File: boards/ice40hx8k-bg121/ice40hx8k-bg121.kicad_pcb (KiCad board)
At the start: 4 copper layers, 22.9 x 48.3 mm, 56 parts, among them J1 Conn_01x16, J2 Conn_01x16, J3 Conn_02x06_Odd_Even, J4 Conn_02x06_Odd_Even, SW1 B3U-1000P, U1 AP7361C-33Y5-13, U2 AP7361C-12Y5-13, U3 iCE40HX8K-BG121(121-Ball_caBG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, U4 LE25U20AMB, U5 ASDMB-xxxMHz

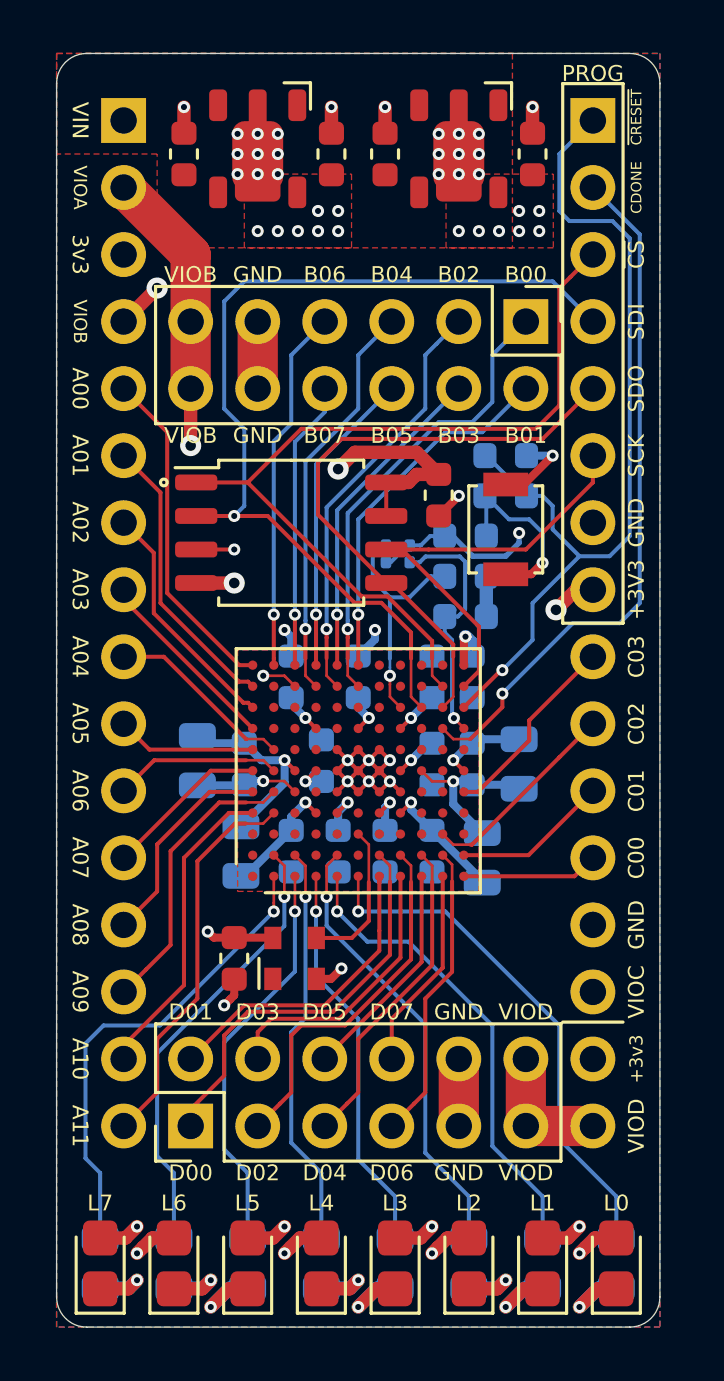
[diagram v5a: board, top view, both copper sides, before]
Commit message: Revert "Updated version info on backside of board."
This reverts commit 1f51933b87c9f3e20d21da3a8fb08a06faebd8ba.
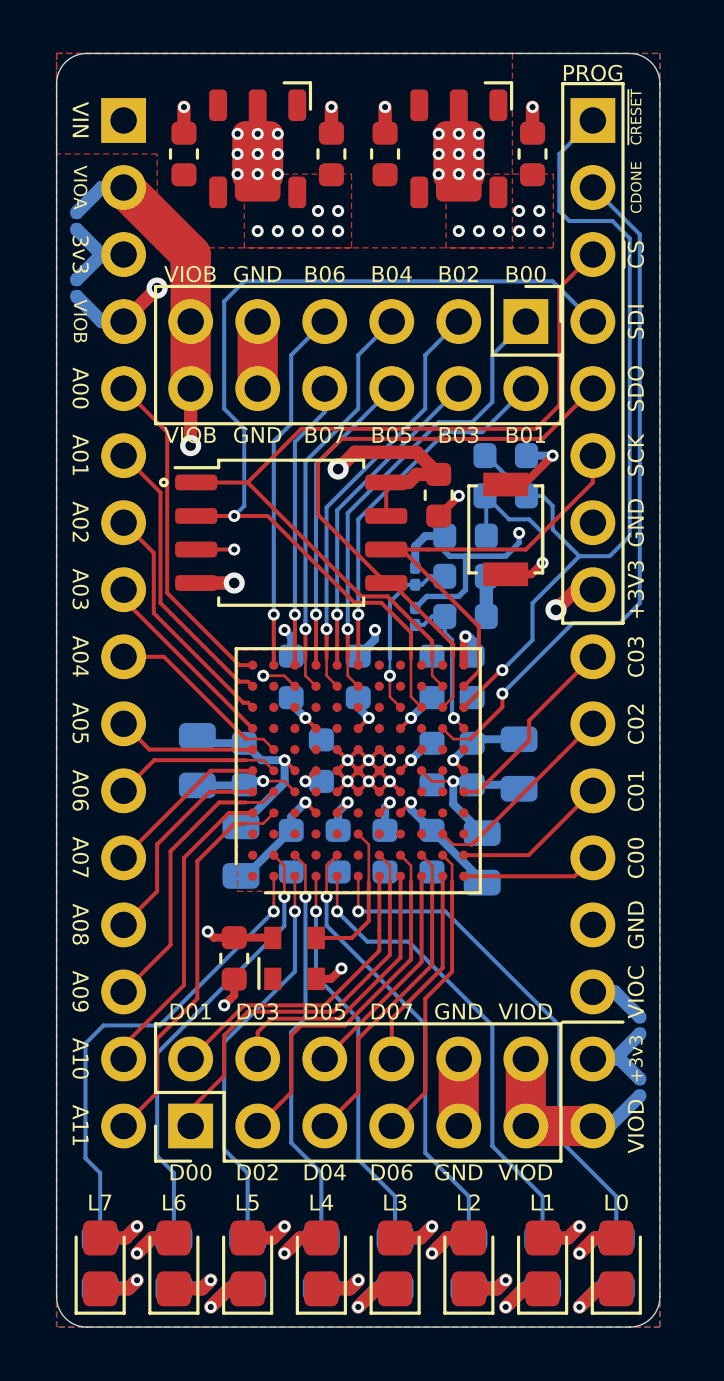
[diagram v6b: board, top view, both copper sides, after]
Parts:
- added JP3: VCCIO_A, jkiv-library:J_NO_0201_0603Metric, B.Cu at (21.1, 24.1)
- added JP4: VCCIO_B, jkiv-library:J_NO_0201_0603Metric, B.Cu at (21.1, 21.6)
- added JP5: VCCIO_C, jkiv-library:J_NO_0201_0603Metric, B.Cu at (42.4, 52.1)
- added JP6: VCCIO_D, jkiv-library:J_NO_0201_0603Metric, B.Cu at (42.4, 54.4)
- moved JP1 2.39 mm to (33.9, 36.6)
- moved JP2 1.40 mm to (33.9, 35.1), turned to 270 degrees
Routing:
- net +3V3: track 36.1 -> 47.1 mm
- net CBSEL0: track 9.55 -> 5.84 mm
- net CBSEL1: track 9.35 -> 6.63 mm
- net VCCIO_D: track 23.3 -> 25.5 mm
- net VCCIO_C: track 15.9 -> 18.1 mm
- net VCCIO_B: track 28.3 -> 30.4 mm
- net VCCIO_A: track 25.4 -> 27.5 mm
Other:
- board text added: "fourside.io"
- board text added: "ice40hx8k breakout 2020-03"
- board text removed: "(cc) fourside.io"
- board text removed: "ice40hx8k breakout 2020-04"

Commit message: [ice40hx8k-bg121] Updated design rules. Passes DRC.
Updated design rules. Adjusted soldermask clearance ratio.
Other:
- rule trace_min: 0.0889 -> 0.09
- rule via_min_size: 0.23 -> 0.45
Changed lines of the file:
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@@
     (zone_clearance 0.1016)
     (zone_45_only no)
-    (trace_min 0.0889)
+    (trace_min 0.09)
     (via_size 0.8)
     (via_drill 0.4)
-    (via_min_size 0.23)
+    (via_min_size 0.45)
     (via_min_drill 0.2)
     (user_via 0.4572 0.2286)
@@
     (pad_to_mask_clearance 0.051)
     (solder_mask_min_width 0.25)
+    (pad_to_paste_clearance_ratio -0.15)
     (aux_axis_origin 0 0)
     (visible_elements 7FFFFFFF)
@@
     (add_net VCCIO_D)
   )
+  (module jkiv-library:J_NO_0201_0603Metric (layer B.Cu)
+    (at 33.909 35.052 270)
+    (descr "Resistor SMD 0201 (0603 Metric), square (rectangular) end terminal, IPC_7351 nominal, (Body size source: https://www.vishay.com/docs/20052/crcw0201e3.pdf), generated with kicad-footprint-generator")
+    (tags resistor)
+    (attr smd)
+    (fp_text reference JP2 (at 0 0.254 90) (layer B.SilkS) hide
+      (effects (font (size 1 1) (thickness 0.15)) (justify mirror))
+    )
+    (fp_text value CBSEL0 (at 0 -1.05 90) (layer B.Fab)
+      (effects (font (size 1 1) (thickness 0.15)) (justify mirror))
+    )
+    (fp_line (start -0.6 -0.3) (end -0.6 0.3) (layer B.SilkS) (width 0.12))
+    (fp_line (start 0.6 -0.3) (end -0.6 -0.3) (layer B.SilkS) (width 0.12))
+    (fp_line (start 0.6 0.3) (end 0.6 -0.3) (layer B.SilkS) (width 0.12))
+    (fp_line (start -0.6 0.3) (end 0.6 0.3) (layer B.SilkS) (width 0.12))
+    (fp_poly (pts (xy -0.2 0.1) (xy 0.2 0.1) (xy 0.2 -0.1) (xy -0.2 -0.1)) (layer B.Mask) (width 0.1))
+    (fp_text user %R (at 0 0.68 90) (layer B.Fab)
+      (effects (font (size 0.25 0.25) (thickness 0.04)) (justify mirror))
+    )
+    (fp_line (start 0.3 0.15) (end 0.3 -0.15) (layer B.Fab) (width 0.1))
+    (fp_line (start -0.3 -0.15) (end -0.3 0.15) (layer B.Fab) (width 0.1))
+    (pad 2 smd roundrect (at 0.32 0 270) (size 0.46 0.4) (layers B.Cu B.Mask) (roundrect_rratio 0.25)
+      (net 98 CBSEL1) (solder_paste_margin_ratio -0.5))
+    (pad 1 smd roundrect (at -0.32 0 270) (size 0.46 0.4) (layers B.Cu B.Mask) (roundrect_rratio 0.25)
+      (net 2 +3V3) (solder_paste_margin_ratio -0.5))
+    (pad "" smd roundrect (at 0.345 0 270) (size 0.318 0.36) (layers B.Paste) (roundrect_rratio 0.25))
+    (pad "" smd roundrect (at -0.345 0 270) (size 0.318 0.36) (layers B.Paste) (roundrect_rratio 0.25))
+  )
   (module Symbol:OSHW-Symbol_6.7x6mm_SilkScreen (layer B.Cu)
     (at 31.75 19.558 180)
@@
   )
   (module jkiv-library:J_NO_0201_0603Metric (layer B.Cu)
-    (at 33.909 35.052 270)
-    (descr "Resistor SMD 0201 (0603 Metric), square (rectangular) end terminal, IPC_7351 nominal, (Body size source: https://www.vishay.com/docs/20052/crcw0201e3.pdf), generated with kicad-footprint-generator")
-    (tags resistor)
-    (attr smd)
-    (fp_text reference JP2 (at 0 0.254 90) (layer B.SilkS) hide
-      (effects (font (size 1 1) (thickness 0.15)) (justify mirror))
-    )
-    (fp_text value CBSEL0 (at 0 -1.05 90) (layer B.Fab)
-      (effects (font (size 1 1) (thickness 0.15)) (justify mirror))
-    )
-    (fp_line (start -0.6 -0.3) (end -0.6 0.3) (layer B.SilkS) (width 0.12))
-    (fp_line (start 0.6 -0.3) (end -0.6 -0.3) (layer B.SilkS) (width 0.12))
-    (fp_line (start 0.6 0.3) (end 0.6 -0.3) (layer B.SilkS) (width 0.12))
-    (fp_line (start -0.6 0.3) (end 0.6 0.3) (layer B.SilkS) (width 0.12))
-    (fp_poly (pts (xy -0.2 0.1) (xy 0.2 0.1) (xy 0.2 -0.1) (xy -0.2 -0.1)) (layer B.Mask) (width 0.1))
-    (fp_text user %R (at 0 0.68 90) (layer B.Fab)
-      (effects (font (size 0.25 0.25) (thickness 0.04)) (justify mirror))
-    )
-    (fp_line (start 0.3 0.15) (end 0.3 -0.15) (layer B.Fab) (width 0.1))
-    (fp_line (start -0.3 -0.15) (end -0.3 0.15) (layer B.Fab) (width 0.1))
-    (pad 2 smd roundrect (at 0.32 0 270) (size 0.46 0.4) (layers B.Cu B.Mask) (roundrect_rratio 0.25)
-      (net 98 CBSEL1) (solder_paste_margin_ratio -0.5))
-    (pad 1 smd roundrect (at -0.32 0 270) (size 0.46 0.4) (layers B.Cu B.Mask) (roundrect_rratio 0.25)
-      (net 2 +3V3) (solder_paste_margin_ratio -0.5))
-    (pad "" smd roundrect (at 0.345 0 270) (size 0.318 0.36) (layers B.Paste) (roundrect_rratio 0.25))
-    (pad "" smd roundrect (at -0.345 0 270) (size 0.318 0.36) (layers B.Paste) (roundrect_rratio 0.25))
-  )
-  (module jkiv-library:J_NO_0201_0603Metric (layer B.Cu)

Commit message: Updated sheet info, gerbers, BOMs.
* ft2232h-ice40
* ice40hx8k-bg121 breakout
* atsamd21e18a
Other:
- board text added: "ice40hx8k breakout 2020-04"
- board text removed: "ice40hx8k breakout 2020-03"
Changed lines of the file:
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@@
   )
   (page A4)
+  (title_block
+    (title "ice40hx8k-bg121 Breakout")
+    (date 2020-11-09)
+    (rev 2020-04)
+    (company fourside.io)
+  )
   (layers
     (0 F.Cu signal)
@@
     (pcbplotparams
       (layerselection 0x010fc_ffffffff)
-      (usegerberextensions true)
+      (usegerberextensions false)
       (usegerberattributes false)
-      (usegerberadvancedattributes true)
+      (usegerberadvancedattributes false)
       (creategerberjobfile false)
       (excludeedgelayer true)
@@
       (psa4output false)
       (plotreference true)
-      (plotvalue true)
+      (plotvalue false)
       (plotinvisibletext false)
-      (padsonsilk false)
+      (padsonsilk true)
       (subtractmaskfromsilk true)
       (outputformat 1)
@@
     (effects (font (size 0.4 0.4) (thickness 0.1)) (justify mirror))
   )
-  (gr_text "ice40hx8k breakout\n2020-03" (at 31.623 50.546) (layer B.SilkS)
+  (gr_text "ice40hx8k breakout\n2020-04" (at 31.623 50.546) (layer B.SilkS)
     (effects (font (size 0.8 0.8) (thickness 0.1)) (justify mirror))
   )
